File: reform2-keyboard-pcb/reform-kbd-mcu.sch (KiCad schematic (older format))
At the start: 33 parts, among them J1 USB, J2 UART, J3 AUX, J4 USB_C_Receptacle_USB2.0, SW83 RESET, SW84 SW_DIP_x01, U1 ATMEGA32U4-AU, U3 MCP1700-3302E_SOT23, Y1 16MHz

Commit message: reform2: update PCBs incl. badges to production revs, add keyboard lettering, misc docs
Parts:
- added D164: BZT52-B5V6J, Diode_SMD:D_SOD-123, symbol Diode:BZT52Bxx
- added F1: 0ZCJ0075AF2E, Resistor_SMD:R_1206_3216Metric, symbol Device:Polyfuse_Small
- added FB1: BLM18PG221SH1D, Inductor_SMD:L_0603_1608Metric, symbol Device:Ferrite_Bead_Small
- added GFX3: MNT, reform2-keyboard:mntreform-keyboard-badge, symbol Mechanical:MountingHole
- added R15: 0, Resistor_SMD:R_0603_1608Metric, symbol Device:R_Small
- added U4: USBLC6-2SC6, Package_TO_SOT_SMD:SOT-23-6, symbol Power_Protection:USBLC6-2SC6
- C11, C12, R13, R14, U3: Flags DNP -> (none)
- J4: symbol Connector:USB_C_Receptacle_USB2.0 -> reform2-keyboard-rescue:USB_C_Receptacle_USB2.0-Connector; Flags DNP -> (none)
- R1, R2: Manufacturer Vishay Dale -> Yageo; Manufacturer_No CRCW06030000Z0EAC -> RC0603FR-0722RL
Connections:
- net labels added: HD+, HD-
- wire segments 111 -> 138
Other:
- note added: "To SYSCTL"
- note removed: "lid sensor was SM351LT"
- moved on the sheet: C1, C11, C12, C2, C3, C4, C5, C6, GFX1, GFX2, H1, H2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

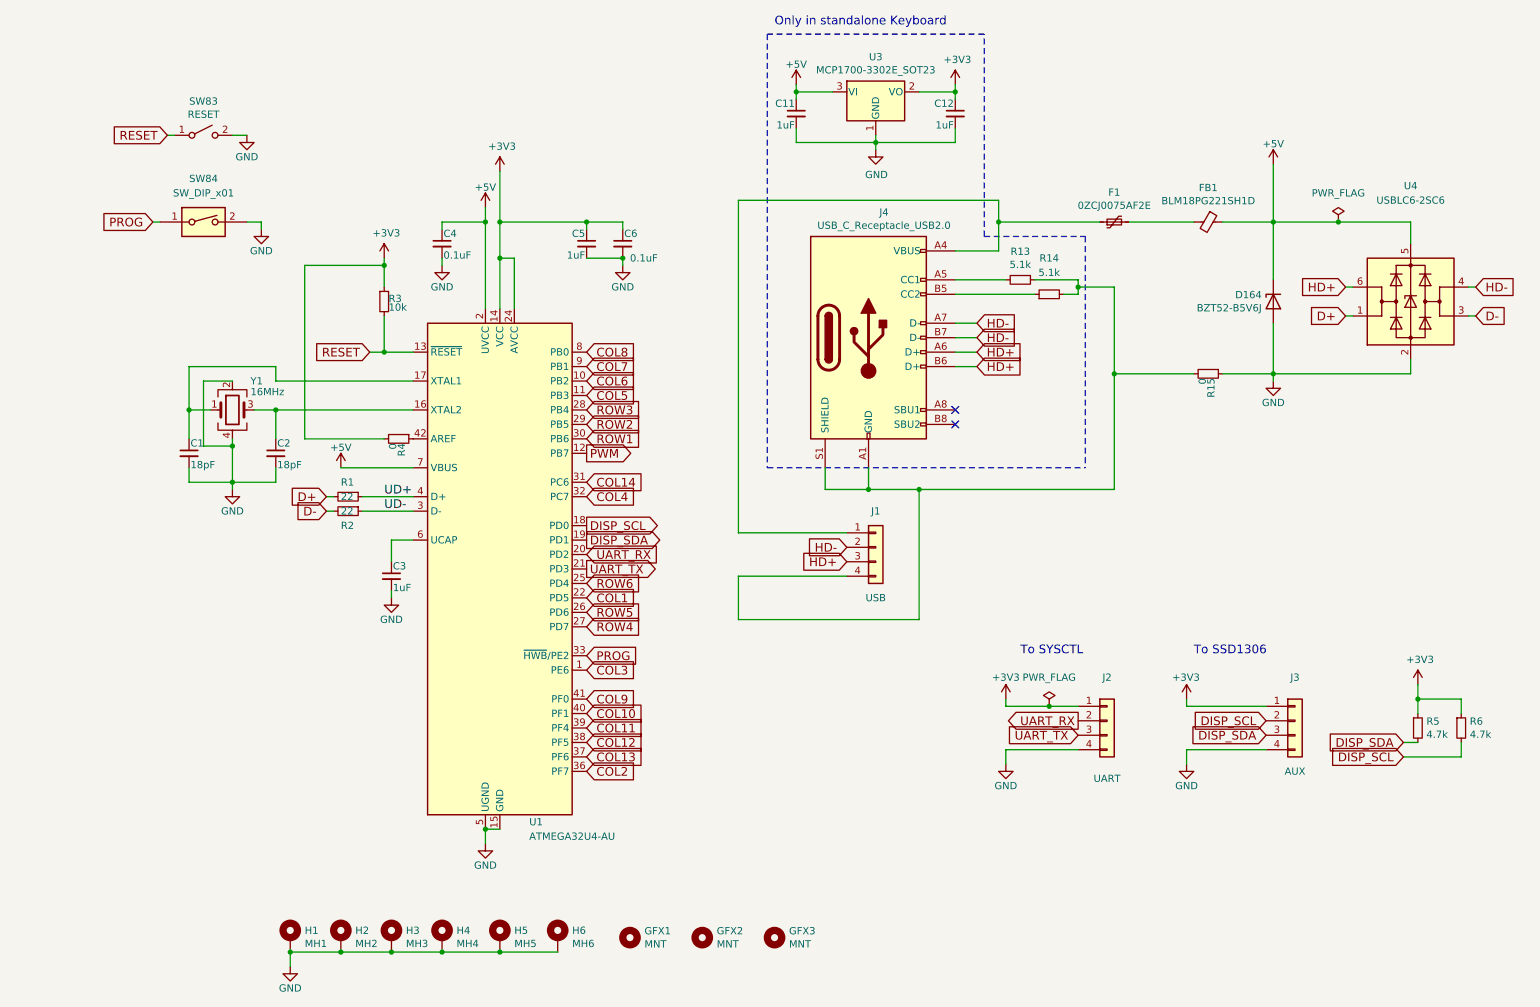
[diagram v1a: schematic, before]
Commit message: keyboard: add pcb version that has almost all components on the front side, with parts from lcsc
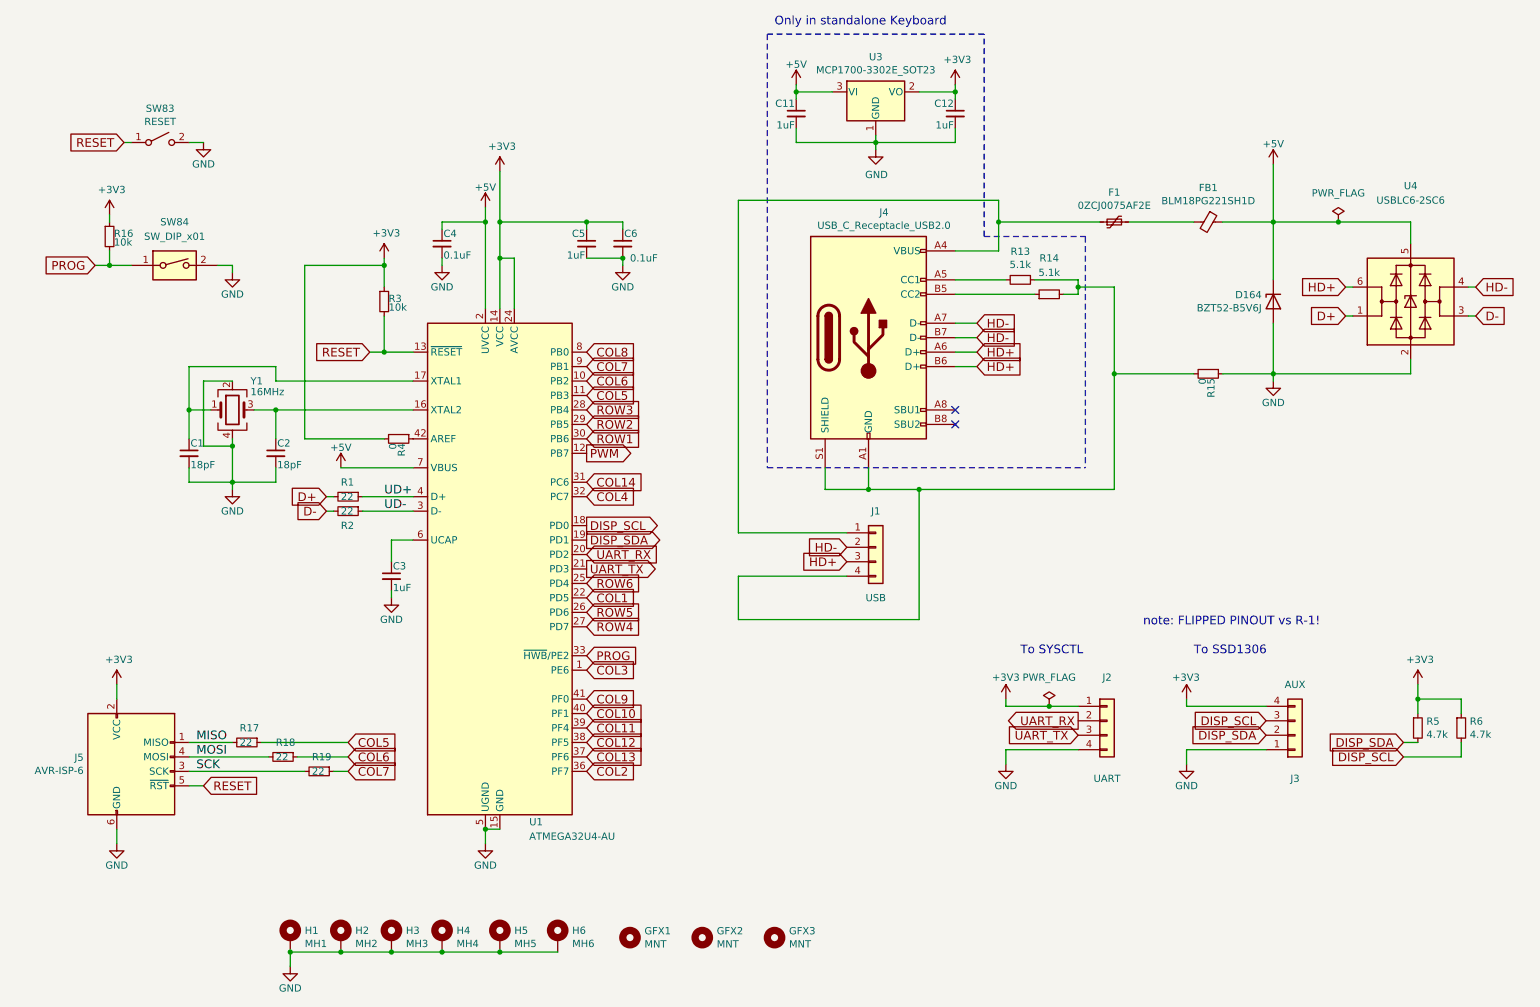
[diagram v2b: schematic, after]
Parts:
- added J5: AVR-ISP-6, Connector_PinHeader_2.54mm:PinHeader_2x03_P2.54mm_Vertical, symbol Connector:AVR-ISP-6
- added R16: 10k, Resistor_SMD:R_0603_1608Metric, symbol Device:R_Small
- added R17, R18, R19: 22, Resistor_SMD:R_0603_1608Metric, symbol Device:R_Small
- C1, C2: LCSC (none) -> C107040
- C11, C12, C3, C5: LCSC (none) -> C14664; Manufacturer TDK -> Yageo; Manufacturer_No C1608X8L1C105K080AC -> CC0603KRX5R8BB105
- C4, C6: LCSC (none) -> C14663; Manufacturer_No CC0603JPX7R9BB104 -> CC0603KRX7R9BB104
- D164: Alt MPN (none) -> BZT52-B5V6J; Alt Manuf (none) -> Nexperia; LCSC (none) -> C173406; Manufacturer Nexperia -> MDD; Manufacturer_No BZT52-B5V6J -> BZT52C5V6
- F1: Alt MPN (none) -> 0ZCJ0075AF2E; Alt Manuf (none) -> Bel Fuse; LCSC (none) -> C70082; Manufacturer Bel Fuse -> TECHFUSE; Manufacturer_No 0ZCJ0075AF2E -> nSMD100-16V
- FB1: LCSC (none) -> C14709; Manufacturer_No BLM18PG221SH1D -> BLM18PG121SN1D
- GFX1, GFX2, H1, H2, H3, H4, H5, H6: Flags (none) -> DNP; Manufacturer (none) -> DNP; Manufacturer_No (none) -> DNP
- GFX3: footprint reform2-keyboard:mntreform-keyboard-badge -> footprints:mnt-reform-keyboard-r2-badge; Flags (none) -> DNP; Manufacturer (none) -> DNP; Manufacturer_No (none) -> DNP
- J1, J2: Alt MPN (none) -> 62000411622; Alt Manuf (none) -> Würth; LCSC (none) -> C265332; Manufacturer_No S4B-PH-SM4-TB(LF)(SN) -> S4B-PH-SM4-K-TB(LF)(SN)
- J3: Alt MPN (none) -> 686104148922; Alt Manuf (none) -> Würth; LCSC (none) -> C555410; Manufacturer Molex -> XFCN; Manufacturer_No 200528-0040 -> F1002-B-04-20T-R
- J4: footprint Connector_USB:USB_C_Receptacle_Amphenol_12401610E4-2A -> Connector_USB:USB_C_Receptacle_HRO_TYPE-C-31-M-12; LCSC (none) -> C165948; Manufacturer Amphenol -> Korean Hroparts; Manufacturer_No 12401610E4#2A -> TYPE-C-31-M-12
- R1, R2: LCSC (none) -> C107701
- R13, R14: LCSC (none) -> C105580; Manufacturer Panasonic -> Yageo; Manufacturer_No ERJ-3EKF5101V -> RC0603FR-075K1L
- R15, R4: LCSC (none) -> C95177; Manufacturer Vishay Dale -> Yageo; Manufacturer_No CRCW06030000Z0EAC -> RC0603JR-070RL
- R3: LCSC (none) -> C99198; Manufacturer_No RC0603FR-0710KL -> RC0603JR-0710KL
- R5, R6: LCSC (none) -> C105428; Manufacturer_No RC0603FR-074K7L -> RC0603JR-074K7L
- SW83: Alt MPN (none) -> KMR221GLFS; Alt Manuf (none) -> C&K; LCSC (none) -> C318893; Manufacturer C&K -> XKB; Manufacturer_No KMR221GLFS -> TS-1185EC-C-D-B
- SW84: Alt MPN (none) -> 418121270801; Alt Manuf (none) -> Würth; LCSC (none) -> C402914; Manufacturer Apem -> Dongguan Guangzhu; Manufacturer_No DM01 -> DSIC01LSGET
- U1: Manufacturer_No ATMEGA32U4-AU -> ATMEGA32U4-AU / RC
- U3: LCSC (none) -> C39051
- U4: Alt MPN (none) -> USBLC6-2SC6; Alt Manuf (none) -> STMicroelectronics; LCSC (none) -> C2687116; Manufacturer STMicroelectronics -> UMW
- Y1: Alt MPN (none) -> ABM8AIG-16.000MHz-4-T; Alt Manuf (none) -> Abracon; LCSC (none) -> C70562; Manufacturer Abracon -> Yangxing; Manufacturer_No ABM8AIG-16.000MHz-4-T -> X322516MRB4SI
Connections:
- net +3V3: now also J3.4 (Pin_4), J5.2 (VCC), R16.1; no longer J3.1 (Pin_1)
- net COL5: now also R17.1
- net COL6: now also R18.1
- net COL7: now also R19.1
- net DISP_SCL: now also J3.3 (Pin_3); no longer J3.2 (Pin_2)
- net DISP_SDA: now also J3.2 (Pin_2); no longer J3.3 (Pin_3)
- net GND: now also J3.1 (Pin_1), J5.6 (GND); no longer J3.4 (Pin_4)
- net PROG: now also R16.2
- net RESET: now also J5.5 (~RST)
- new net MISO: J5.1 (MISO), R17.2
- new net MOSI: J5.4 (MOSI), R18.2
- new net SCK: J5.3 (SCK), R19.2
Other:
- note added: "note: FLIPPED PINOUT vs R-1!"
- moved on the sheet: SW83, SW84
